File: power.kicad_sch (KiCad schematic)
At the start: 61 parts, among them J1 PWR + CAN harness, Q1 100V 6.8mOhm N-ch, U1 LM74700-Q1, U2 LM5164 (5V), U3 LM5164 (3V3)

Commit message: Power-fail ride-through: detect, coast, shed; board grows to 84 x 100
The ignition cuts this board's power with a log file open, every drive.
Three new pieces make that survivable, all simulated before layout:

- Detect: TLV431 + 100k/12.7k divider on VBAT_F, AHEAD of the ideal
  diode, asserting PWR_FAIL (IO15) at 11.0 V with ~0.3 V hysteresis.
  The harness collapses microseconds after the key turns while +VBAT
  coasts, so the warning costs no stored energy.
- Coast: two 220 uF/100 V cans join the 100 uF on +VBAT. 540 uF on the
  input rail, where a volt of headroom is worth most.
- Shed: AO3401 + 2N7002 high-side switch on the sensor rail (SENS_EN,
  IO16, off at reset), with PF1 moved behind it so a tripped sensor
  fuse can also be power-cycled from firmware.

Simulated end to end: detection <1 ms after the cut, then 108 ms to
converter dropout with sensors shed, 53 ms without -- the switch doubles
the flush budget. ISO pulse 1's brownout shortens from 8.2 to 5.6 ms.

The two cans plus the detector had no free board left on 84 x 84, so the
board grows to 84 x 100 (still JLC's cheap tier): bottom-edge furniture
and mounting holes move down 16 mm, one can per side, and the detector/
switch column gets its own placement zone. Also included from the audit:
the 3V3 buck's own input capacitor pair at its VIN pin (it was reaching
12.6 mm across to the 5 V island's), the CAN transceiver and AHCT buffer
bypasses pinned at their pins, and Power-class tracks at 0.55 mm to clear
IPC-2221 for 2 A at a 20 C rise.

Hard-won generator fix: a literal newline inside a symbol property is
accepted by KiCad's loader but silently breaks connectivity for every
symbol after it in the file -- the netlist dropped 45 components with no
error pointing anywhere near the cause. The emitter now flattens all
whitespace in property strings.

Board: 0 DRC violations, 0 unconnected, physical audit clean end to end.
185 components, 111 nets, ERC clean, netlist verified node-for-node.

Co-Authore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
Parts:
- added C21: 270pF, Capacitor_SMD:C_0805_2012Metric, symbol Device:C
- added C22, C23: 22uF, Capacitor_SMD:C_1206_3216Metric, symbol Device:C
- added C24: 100nF, Capacitor_SMD:C_0805_2012Metric, symbol Device:C
- added C25: 10uF, Capacitor_SMD:C_1206_3216Metric, symbol Device:C
- added Q2: P-ch 30V 3A, Package_TO_SOT_SMD:SOT-23, symbol Transistor_FET:Q_PMOS_GSD
- added Q3: N-ch 60V 200mA, Package_TO_SOT_SMD:SOT-23, symbol Transistor_FET:Q_NMOS_GSD
- added R16, R18, R21: 100k, Resistor_SMD:R_0805_2012Metric, symbol Device:R
- added R17: 20.5k, Resistor_SMD:R_0805_2012Metric, symbol Device:R
- added R19: 57.6k, Resistor_SMD:R_0805_2012Metric, symbol Device:R
- added R20: 95.3k, Resistor_SMD:R_0805_2012Metric, symbol Device:R
- added R22: 1k, Resistor_SMD:R_0805_2012Metric, symbol Device:R
- added U4: LM5164 (3V3), Package_SO:SOIC-8-1EP_3.9x4.9mm_P1.27mm_EP2.95x4.9mm_Mask2.71x3.4mm_ThermalVias, symbol Regulator_Switching:LM5164DDA
- C10: value 22uF -> 2.2nF; footprint Capacitor_SMD:C_1206_3216Metric -> Capacitor_SMD:C_0805_2012Metric; Note (none) -> Bootstrap: datasheet mandates exactly 2.2nF X7R -- a larger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; Voltage 16V -> 50V
- C11: value 22uF -> 3.3nF; footprint Capacitor_SMD:C_1206_3216Metric -> Capacitor_SMD:C_0805_2012Metric; Note (none) -> Ramp capacitor CA; Voltage 16V -> 50V
- C12: value 100nF -> 270pF; Note (none) -> Ramp coupling capacitor CB; Voltage 16V -> 50V
- C13: value 10nF -> 22uF; footprint Capacitor_SMD:C_0805_2012Metric -> Capacitor_SMD:C_1206_3216Metric; Note EN noise immunity, as for the 5V rail -> (none); Voltage 100V -> 16V
- C14: value 2.2nF -> 22uF; footprint Capacitor_SMD:C_0805_2012Metric -> Capacitor_SMD:C_1206_3216Metric; Note Bootstrap: datasheet-mandated 2.2nF X7R, do not increase -> (none); Voltage 50V -> 16V
- C15: value 3.3nF -> 100nF; Note Ramp capacitor CA -> (none); Voltage 50V -> 16V
- C16: value 270pF -> 100nF; Note Ramp coupling capacitor CB -> 3V3 buck HF input bypass -- must sit at U3's VIN pin; Voltage 50V -> 100V
- C17: value 22uF -> 10uF; Note (none) -> 3V3 buck bulk input, at the VIN pin; Voltage 16V -> 100V
- C18: value 22uF -> 10nF; footprint Capacitor_SMD:C_1206_3216Metric -> Capacitor_SMD:C_0805_2012Metric; Note (none) -> EN noise immunity, as for the 5V rail; Voltage 16V -> 100V
- C19: value 100nF -> 2.2nF; Note (none) -> Bootstrap: datasheet-mandated 2.2nF X7R, do not increase; Voltage 16V -> 50V
- C20: value 10uF -> 3.3nF; footprint Capacitor_SMD:C_1206_3216Metric -> Capacitor_SMD:C_0805_2012Metric; Note (none) -> Ramp capacitor CA; Voltage 16V -> 50V
- C6: value 10nF -> 220uF; footprint Capacitor_SMD:C_0805_2012Metric -> Capacitor_SMD:CP_Elec_16x17.5; symbol Device:C -> Device:C_Polarized; Note EN sits on a bare 100k to VBAT; this keeps a high-impedance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 -> Power-fail ride-through. With the sensor rail shed and the 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
- C7: value 2.2nF -> 220uF; footprint Capacitor_SMD:C_0805_2012Metric -> Capacitor_SMD:CP_Elec_16x17.5; symbol Device:C -> Device:C_Polarized; Note Bootstrap: datasheet mandates exactly 2.2nF X7R -- a larger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 -> Power-fail ride-through. With the sensor rail shed and the 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; Voltage 50V -> 100V
- C8: value 3.3nF -> 1nF; Note Ramp capacitor CA -> Just enough to keep switching noise off the reference. Larg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
- C9: value 270pF -> 10nF; Note Ramp coupling capacitor CB -> EN sits on a bare 100k to VBAT; this keeps a high-impedance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; Voltage 50V -> 100V
- PF1: Note Resettable: a shorted sensor wire trips this, not the board -> Resettable: a shorted sensor wire trips this, not the board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
- R10: value 20.5k -> 100k; Note RON = 3.3V x 2500 / 400kHz (Eq 12) -> 402kHz; tON = 154ns a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 -> Enable tied to VIN (LM74700 already gates on UVLO)
- R11: value 100k -> 31.6k; Note FB upper: 1.2V ref -> 3.28V -> RON = 5.0V x 2500 / 400kHz (Eq 12) -> 396kHz; tON = 237ns a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
- R12: value 57.6k -> 100k; Note FB lower -> FB upper: 1.2V ref -> 5.00V
- R13: value 95.3k -> 31.6k; Note Ripple-injection ramp resistor RA -> FB lower
- R14: value 100k -> 121k; Note (none) -> Ripple-injection ramp resistor RA
- R15: value 1k -> 100k; Note (none) -> Power-good pull-up
- R3: Note Enable tied to VIN (LM74700 already gates on UVLO) -> Power-fail divider, upper leg; Tolerance (none) -> 1%
- R4: value 31.6k -> 12.7k; Note RON = 5.0V x 2500 / 400kHz (Eq 12) -> 396kHz; tON = 237ns a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 -> Lower leg: trips at 1.24V * 112.7/12.7 = 11.00V on the harn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; Tolerance (none) -> 1%
- R5: value 100k -> 10k; Note FB upper: 1.2V ref -> 5.00V -> Cathode pull-up. 10k gives the part 330uA, over the TLV431'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
- R6: value 31.6k -> 1M; Note FB lower -> Hysteresis, about 0.3V at the harness. Without it a battery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
- R7: value 121k -> 100k; Note Ripple-injection ramp resistor RA -> Holds the switch off when nothing drives it
- R8: value 100k -> 10k; Note Power-good pull-up -> GPIO series/gate resistor
- R9: Note (none) -> Holds the level shifter off while the MCU is in reset
- U2: value LM5164 (5V) -> TLV431A; footprint Package_SO:SOIC-8-1EP_3.9x4.9mm_P1.27mm_EP2.95x4.9mm_Mask2.71x3.4mm_ThermalVias -> Package_TO_SOT_SMD:SOT-23; symbol Regulator_Switching:LM5164DDA -> Reference_Voltage:TL431DBZ; MPN LM5164DDAR -> TLV431ASN1T1G; Note 100V synchronous buck, ultra-low Iq. Non-automotive variant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 -> Power-fail comparator. Below the trip point it stops conduc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
- U3: value LM5164 (3V3) -> LM5164 (5V); Note Second buck straight off the battery: a shorted 5V sensor h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 -> 100V synchronous buck, ultra-low Iq. Non-automotive variant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
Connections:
- net +3V3: now also C20.2, R15.2, R5.1, C22.1, C23.1, C24.1, R18.1, R21.2; no longer C15.2, C17.1, C18.1, C19.1, R11.1, R14.2, R8.2
- net +5V: now also C11.2, C13.1, C14.1, C15.1, R12.1, R7.1, Q2.2 (S); no longer C10.1, C11.1, C12.1, C8.2, PF1.1, R5.1
- net +5VS: now also C25.1; no longer C20.1
- net +VBAT: now also C16.1, C17.1, C6.1, C7.1, R10.1, R16.1, U4.2 (VIN); no longer R3.1, R9.1, U2.2 (VIN)
- net BST_3V3: now also C19.1, U4.7 (BST); no longer C14.1, U3.7 (BST)
- net BST_5V: now also C10.1, U3.7 (BST); no longer C7.1, U2.7 (BST)
- net EN_3V3: now also C18.1, R16.2, U4.3 (EN/UVLO); no longer C13.1, R9.2, U3.3 (EN/UVLO)
- net EN_5V: now also C9.1, R10.2, U3.3 (EN/UVLO); no longer C6.1, R3.2, U2.3 (EN/UVLO)
- net FB_3V3: now also C21.2, R18.2, R19.1, U4.5 (FB); no longer C16.2, R11.2, R12.1, U3.5 (FB)
- net FB_5V: now also C12.2, R12.2, R13.1, U3.5 (FB); no longer C9.2, R5.2, R6.1, U2.5 (FB)
- net GND: now also C14.2, C15.2, C16.2, C7.2, C8.2, C9.2, R11.2, R13.2, R9.2, U2.3 (A), C22.2, C23.2, C24.2, C25.2, Q3.2 (S), R17.2, R19.2, R22.2, U4.1 (GND), U4.9 (EP); no longer C10.2, C11.2, C12.2, C19.2, C20.2, R10.2, R12.2, R15.2, R6.2, U2.1 (GND), U2.9 (EP)
- net PG_3V3: now also R21.1, U4.6 (PGOOD); no longer R14.1, U3.6 (PGOOD)
- net PG_5V: now also R15.1, U3.6 (PGOOD); no longer R8.1, U2.6 (PGOOD)
- net PWR_LED_K: now also R22.1; no longer R15.1
- net RAMP_3V3: now also C20.1, C21.1, R20.2; no longer C15.1, C16.1, R13.2
- net RAMP_5V: now also C11.1, C12.1, R14.2; no longer C8.1, C9.1, R7.2
- net RON_3V3: now also R17.1, U4.4 (RON); no longer R10.1, U3.4 (RON)
- net RON_5V: now also R11.1, U3.4 (RON); no longer R4.1, U2.4 (RON)
- net SW_3V3: now also C19.2, R20.1, U4.8 (SW); no longer C14.2, R13.1, U3.8 (SW)
- net SW_5V: now also C10.2, R14.1, U3.8 (SW); no longer C7.2, R7.1, U2.8 (SW)
- net VBAT_F: now also R3.1
- new net PFD_SENSE: C8.1, R3.2, R4.1, R6.2, U2.2 (REF)
- new net PWR_FAIL: R5.2, R6.1, U2.1 (K)
- new net SENS_EN: R8.1
- new net SENS_EN_G: Q3.1 (G), R8.2, R9.1
- new net SENS_G: Q2.1 (G), Q3.3 (D), R7.2
- new net VSENS_SW: PF1.1, Q2.3 (D)
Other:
- moved on the sheet: C1, C10, C11, C12, C13, C14, C15, C16, C17, C18, C19, C2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

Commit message: USB OVP, card-slot ESD, SD test points, and a gold-standard schematic
Hardware, all simulation- or review-driven:
- USB overvoltage cutoff: TLV431 + AO3401 + MMBT3906 series switch on
  VBUS, tripping at 5.77 V. Re-simulated: a compliant 5 V source passes
  at 4.99 V, the switch opens at 5.95 V of brick, and the +5V rail never
  exceeds 5.2 V from anything up to 14 V -- where a 9 V brick previously
  drove it to 8.4 V against the TJA1051's 6 V absolute maximum.
  Off-the-shelf OVP parts were rejected first: the TPS25200 class cuts
  off near 7 V, which is no protection for a 6 V limit.
- Two SRV05-4 arrays clamp every microSD card contact (LCSC C13612);
  until now the ESP32's ~2 kV pin diodes were all that stood behind a
  card swapped by hand after every session.
- A second USBLC6 clamps the USB-C CC pins -- the first contacts every
  plug insertion touches, previously landing on bare 5.1k resistors.
- Test points on SD_CLK and SD_CMD, the most likely scope targets at
  bring-up and otherwise reachable only on fine-pitch pads.

The schematic itself was rebuilt to read like a reference design
(RejsaCAN was the benchmark): every circuit is now a hand-drawn block --
power-fail detector, sensor-rail switch, USB OVP, connector pull-
resistor clusters, and a single utility panel for test points, ERC
flags, mounting holes and the power LED. Sentence-length values became
part numbers ("0.2A PTC", "AO3401A", "600R") with ratings kept in
hidden fields, which also answers the external review's value-hygiene
findings. Title blocks carry rev B and a date. The Power sheet shrank
from A2 back to A3 in the process.

gen/README.md now documents the whole pipeline -- stages, the block-
drawing conventions with per-rotation pin geometry, the junction rules,
and the traps (property newlines, off-grid points, anchors keeping
their natural rotation) -- so the next board reuses all of it.

Board: 84 x 100, 0 DRC violations, 0 unconnected, 0 courtyard overlaps,
physical audit clean. BOM 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
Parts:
- FB1: value 600R @ 100MHz 3A -> 600R
- FB2: value 600R @ 100MHz 2A -> 600R
- L1: value 33uH 3A -> 33uH
- L2: value 22uH 3A -> 22uH
- PF1: value 0.2A hold / 0.4A trip -> 0.2A PTC
- Q1: value 100V 6.8mOhm N-ch -> IPD068N10
- Q2: value P-ch 30V 3A -> AO3401A
- Q3: value N-ch 60V 200mA -> 2N7002
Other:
- moved on the sheet: C1, C10, C11, C12, C13, C14, C15, C16, C17, C18, C19, C2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

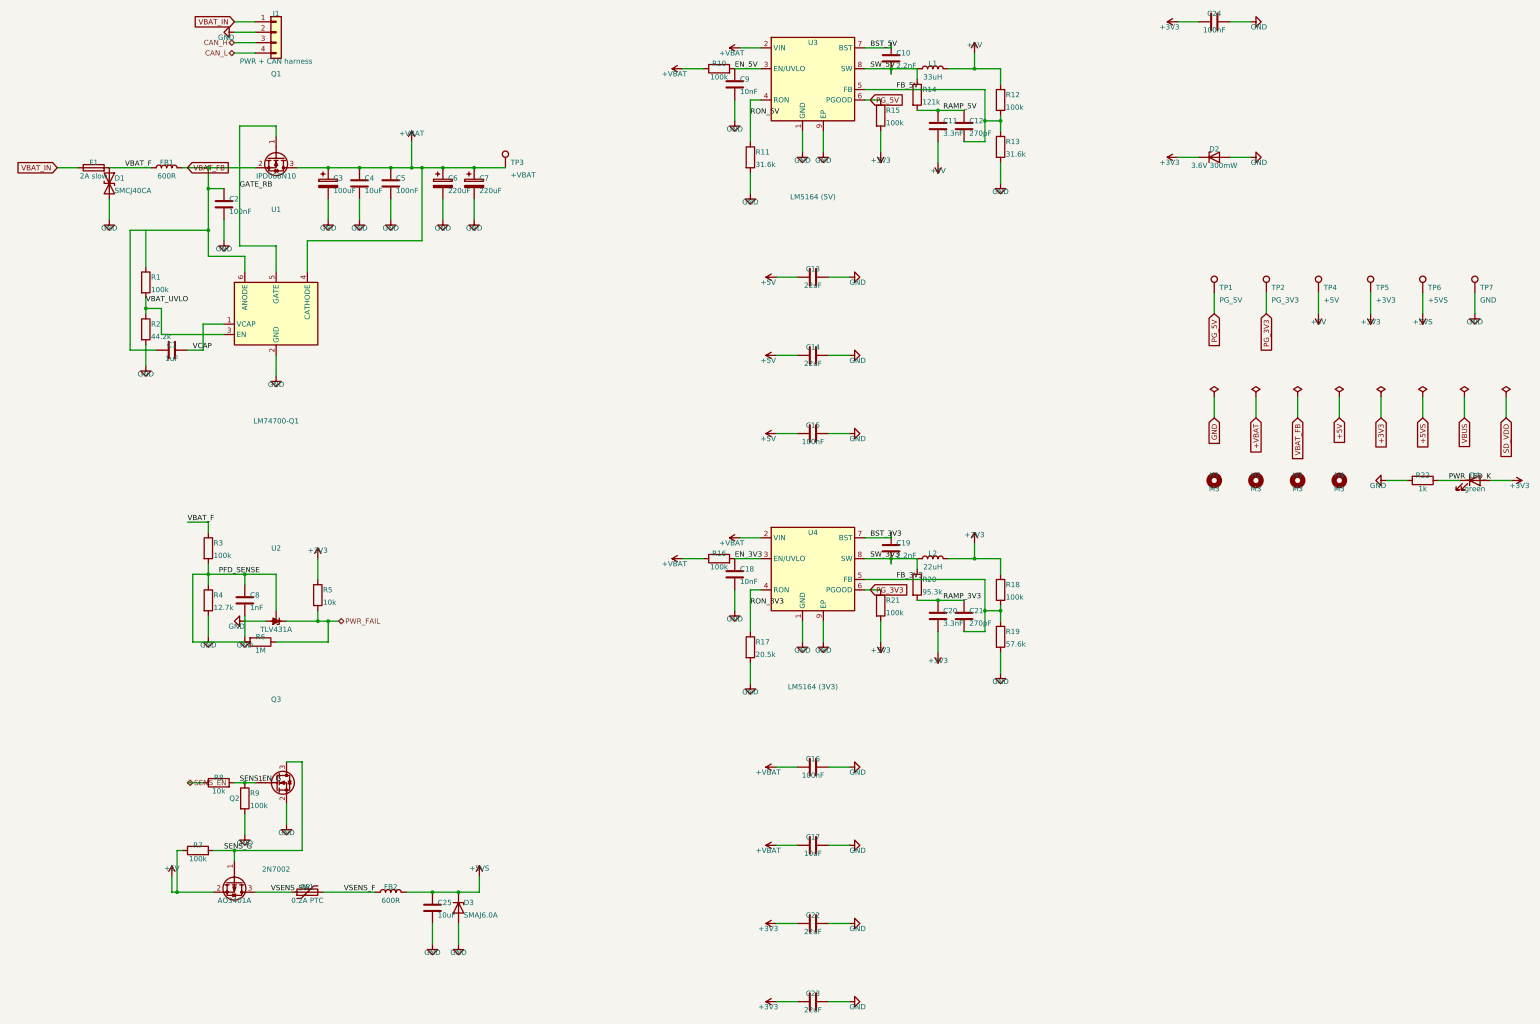
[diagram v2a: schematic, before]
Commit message: Studies 9-11, post-route extraction, strap audit, readable labels, production BOM numbers
New tests, run against the final board:
- audit_routes.py: Dijkstra IR drop over the routed copper (worst 55 mV
  at rated current), SD/USB/CAN routed lengths (USB pair matched to
  1.1 mm), buck switch-node copper area. All clean.
- audit_straps.py: every ESP32-S3 strapping pin against what the netlist
  hangs on it; all five boot in their required state.
- simulate.py 9, stability: the LM5164 ripple-injection criterion across
  the input window. Found the ramp thin (10.6 mV) at a legitimate 8 V
  operating point -- ramp caps changed 3.3 nF -> 2.2 nF, now 15.8 mV+
  everywhere above crank voltages. Board rebuilt: 0 DRC, 0 unconnected,
  0 overlaps.
- simulate.py 10, CAN bus: TJA1051 through the choke and split
  termination into 5 m of terminated line -- 2.00 V dominant at the far
  end, no overshoot.
- simulate.py 11, budgets: enclosure thermal for the in-dash mount
  (sealed ABS is fine in the dash, would exceed the electrolytics' 105 C
  in an engine bay -- documented), fuse derating 69 %, I2C rise time vs
  Qwiic chains, WS2812 count, SD switch drop, connector contacts.
- tolerance MC gains the ride-through corner: 36 ms at caps -20 % /
  load +40 %, still covering a healthy-card flush.

Schematic readability, second pass: net-name labels moved onto short
vertical spurs clear of the circuits (deleting them outright renames
nets to Net-(R5-Pad2) and breaks name-based verification -- now in
gen/README.md), end-labels extend away from what they feed, and the
sensor-switch block redrawn at 1.5x pitch. Reversed-5V behaviour per
connector documented in the README.

BOM production pass: verified LCSC numbers added for the TVS families,
BAT54S, MM3Z zener and 2N7002s (21 numbered lines); the 39 blank lines
are JLC-auto-matched basic R/C; the 12 extended lines that must be
hand-matched in the order UI are listed in README 11. No guessed part
numbers.

gen/README.md gains the readab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
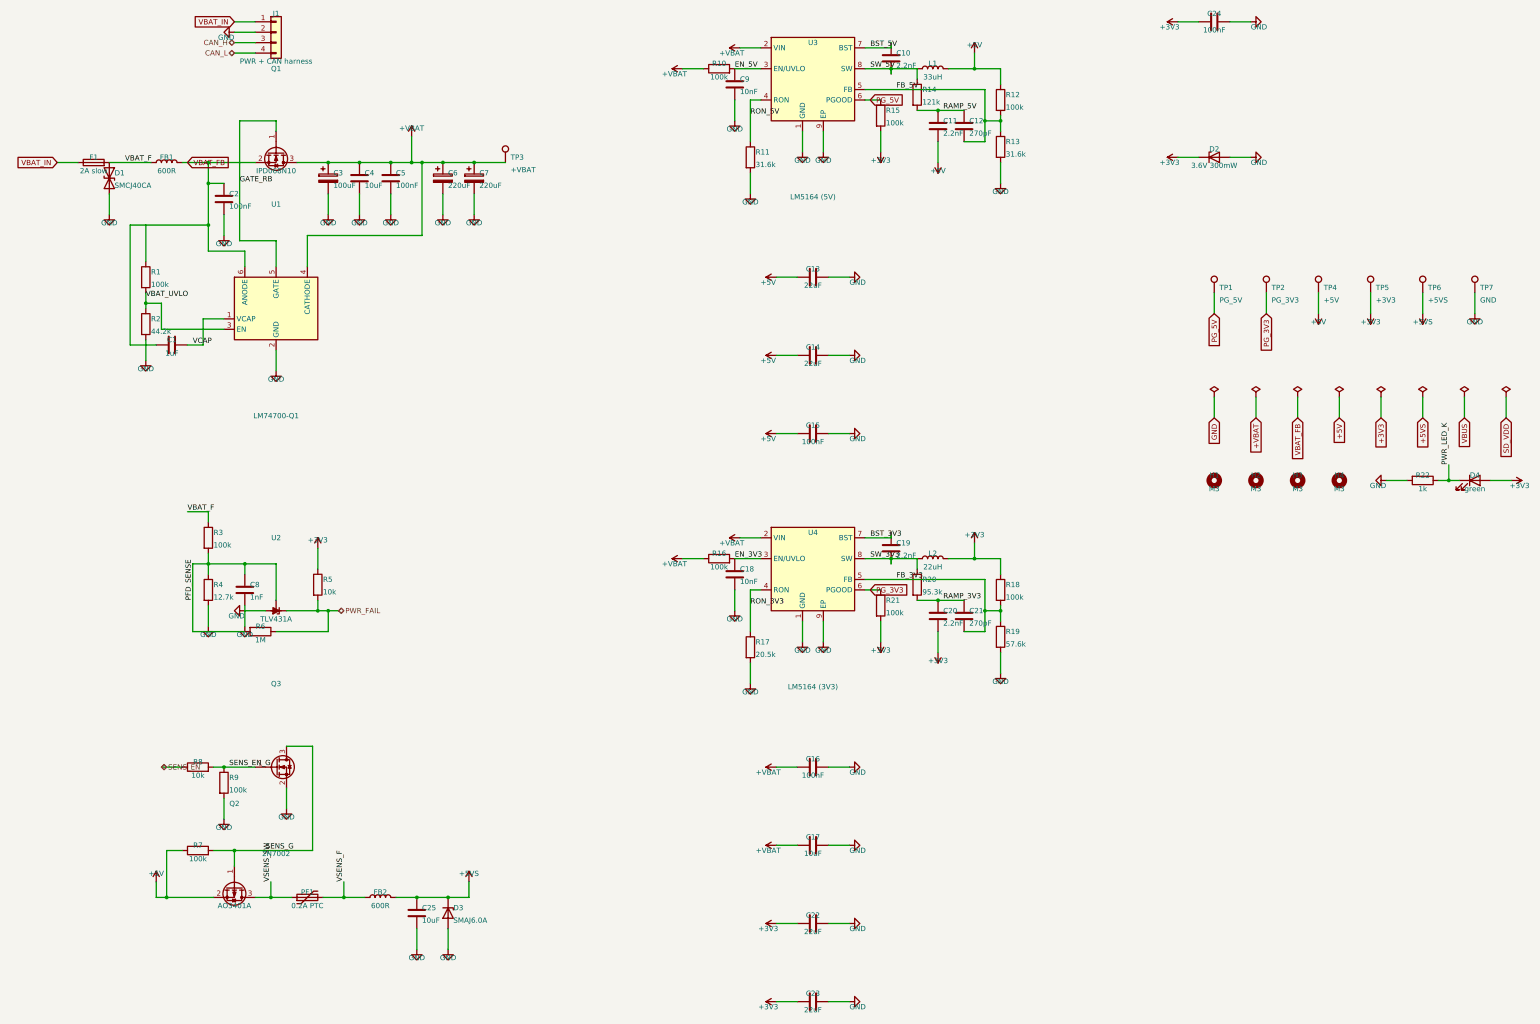
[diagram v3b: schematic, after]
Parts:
- C11: value 3.3nF -> 2.2nF; Note Ramp capacitor CA -> Ramp capacitor CA. 2.2nF, not 3.3nF: at 8 V in the injected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
- C20: value 3.3nF -> 2.2nF; Note Ramp capacitor CA -> Ramp capacitor CA, sized as on the 5 V rail for ramp amplit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
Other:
- moved on the sheet: C1, C2, C25, C3, C4, C5, C6, C7, C8, D1, D3, F1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
